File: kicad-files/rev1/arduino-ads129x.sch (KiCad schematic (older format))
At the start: 186 parts

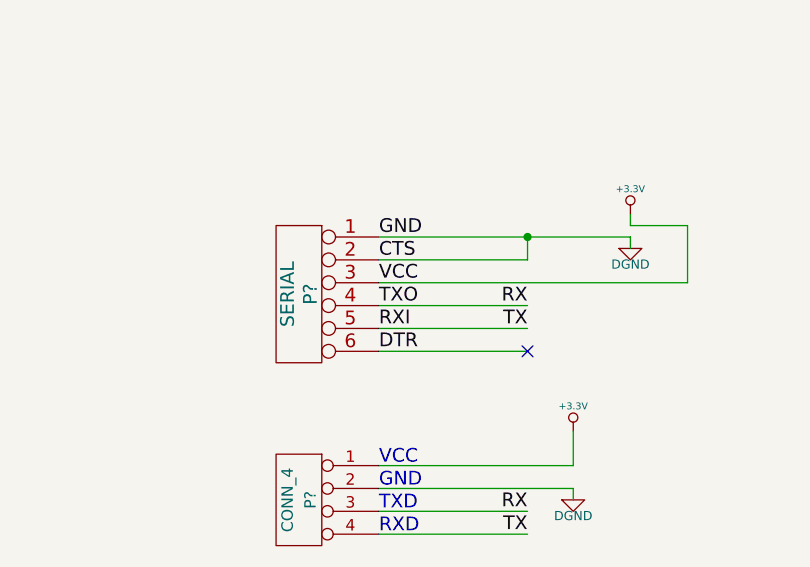
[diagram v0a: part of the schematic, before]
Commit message: replace serial port net-labels with plain text
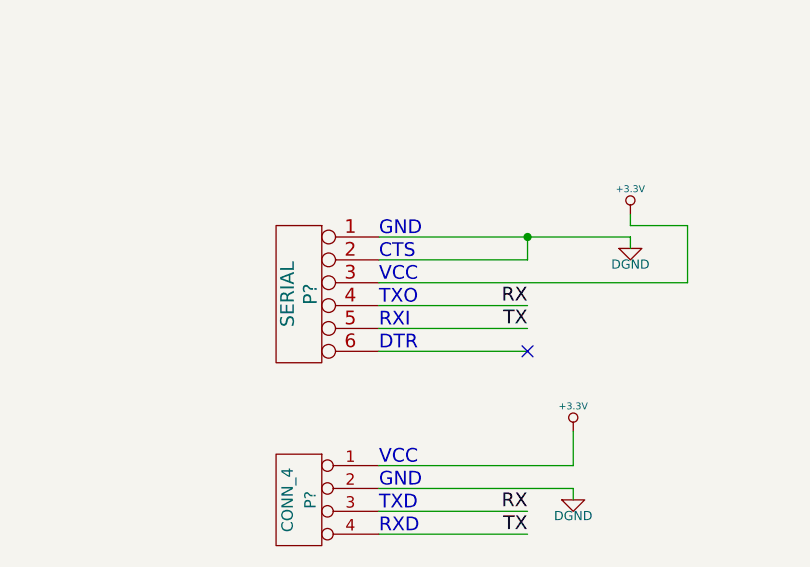
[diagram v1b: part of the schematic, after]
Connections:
- net labels removed: CTS, DTR, RXI, TXO, VCC
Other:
- note added: "CTS"
- note added: "DTR"
- note added: "RXI"
- note added: "TXO"
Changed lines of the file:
@@
-EESchema Schematic File Version 2  date Sat 18 May 2013 03:09:57 PM CEST
+EESchema Schematic File Version 2  date Sat 18 May 2013 03:14:03 PM CEST
 LIBS:power
 LIBS:device
@@
 Comment4 ""
 $EndDescr
+Text Notes 13000 11950 0    60   ~ 0
+DTR
+Text Notes 13000 11850 0    60   ~ 0
+RXI
+Text Notes 13000 11750 0    60   ~ 0
+TXO
+Text Notes 13000 11650 0    60   ~ 0
+VCC
+Text Notes 13000 11550 0    60   ~ 0
+CTS
+Text Notes 13000 11450 0    60   ~ 0
+GND
 Text Label 13650 12750 2    60   ~ 0
 TX
@@
 Text Notes 13000 12450 0    60   ~ 0
 VCC
-Text Label 13000 11450 0    60   ~ 0
-GND
 $Comp
 L CONN_4 P?
@@
 RX
 NoConn ~ 13650 11950
-Text Label 13000 11950 0    60   ~ 0
-DTR
-Text Label 13000 11850 0    60   ~ 0
-RXI
-Text Label 13000 11750 0    60   ~ 0
-TXO
-Text Label 13000 11650 0    60   ~ 0
-VCC
-Text Label 13000 11550 0    60   ~ 0
-CTS
 Text Label 17000 14450 0    60   ~ 0
 RX

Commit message: connect ADS129x to SAM3X
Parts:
- added R? (x4): 10k, symbol R
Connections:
- net labels added: ADS129x_CLK, ADS129x_CLKSEL, ADS129x_CS, ADS129x_DRDY, ADS129x_GPIO1, ADS129x_GPIO2, ADS129x_GPIO3, ADS129x_GPIO4, ADS129x_PWDN, ADS129x_RESET, ADS129x_START, MISO, MOSI, SPCK
- wire segments 678 -> 709
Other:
- note added: "TODO: How do we get the clock divided correctly?"

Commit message: connect ADS129x CLK to SAM3X PA2
 PA2 is labeled AD7 in the Arduino Due schematic
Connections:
- wire segments 709 -> 710
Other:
- note removed: "TODO: How do we get the clock divided correctly?"

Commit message: add yellow and green LEDs for each channel
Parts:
- added D? (x16): LED, symbol LED
- added R? (x8): 68, symbol R
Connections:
- net labels added: GREEN_1, GREEN_2, GREEN_3, GREEN_4, GREEN_5, GREEN_6, GREEN_7, GREEN_8, YELLOW_1, YELLOW_2, YELLOW_3, YELLOW_4, YELLOW_5, YELLOW_6, YELLOW_7, YELLOW_8
- wire segments 710 -> 775

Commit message: add MAYBE note regarding connectors and ground lines
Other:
- note added: "MAYBE double the\nconnectors to \nallow ground lines\ninbetween\nthe signal lines"
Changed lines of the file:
@@
-EESchema Schematic File Version 2  date Sun 19 May 2013 10:32:49 AM CEST
+EESchema Schematic File Version 2  date Sat 25 May 2013 01:05:47 PM CEST
 LIBS:power
 LIBS:device
@@
 Sheet 1 1
 Title ""
-Date "19 may 2013"
+Date "25 may 2013"
 Rev ""
 Comp ""
@@
 Comment4 ""
 $EndDescr
+Text Notes 700  4400 0    60   ~ 0
+MAYBE double the\nconnectors to \nallow ground lines\ninbetween\nthe signal lines
 Text Label 22400 16750 1    60   ~ 0
 GREEN_8

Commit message: make arduino-ads129x header match patch-shield header
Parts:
- removed P?: CONN_10X2, symbol CONN_10X2
- added P?: CONN_20X2, symbol CONN_20X2
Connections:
- net labels removed: VIRTUALGND
- wire segments 775 -> 801
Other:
- note removed: "MAYBE double the\nconnectors to \nallow ground lines\ninbetween\nthe signal lines"

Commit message: move LEDs to patch-shield
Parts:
- removed D? (x16): LED, symbol LED
- removed R? (x8): 68, symbol R
- R?: value 1k -> 560
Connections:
- net labels removed: GREEN_1, GREEN_2, GREEN_3, GREEN_4, GREEN_5, GREEN_6, GREEN_7, GREEN_8, YELLOW_1, YELLOW_2, YELLOW_3, YELLOW_4, YELLOW_5, YELLOW_6, YELLOW_7, YELLOW_8
- wire segments 801 -> 965

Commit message: added shift-out register for LEDs
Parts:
- added P?: CONN_4X2, symbol CONN_4X2
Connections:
- net labels added: LED_LATCH_CLK, LED_OUTPUT_ENABLE_INPUT, LED_SERIAL, LED_SHIFT_REG_CLEAR, LED_SHIFT_REG_CLK
- wire segments 965 -> 984
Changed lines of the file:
@@
-EESchema Schematic File Version 2  date Sat 25 May 2013 04:37:08 PM CEST
+EESchema Schematic File Version 2  date Sat 25 May 2013 05:49:57 PM CEST
 LIBS:power
 LIBS:device
@@
 Comment4 ""
 $EndDescr
+Text Label 16050 12350 0    60   ~ 0
+LED_SERIAL
+Text Label 16050 12500 0    60   ~ 0
+LED_SHIFT_REG_CLK
+Text Label 16050 12650 0    60   ~ 0
+LED_SHIFT_REG_CLEAR
+Text Label 16050 12800 0    60   ~ 0
+LED_LATCH_CLK
+Text Label 16050 13250 0    60   ~ 0
+LED_OUTPUT_ENABLE_INPUT
+Wire Wire Line
+	16050 12800 17700 12800
+Wire Wire Line
+	17700 12500 16050 12500
+Wire Wire Line
+	17700 12350 16050 12350
+Wire Wire Line
+	17700 12650 16050 12650
+Wire Wire Line
+	16050 13250 17700 13250
+$Comp
+L CONN_4X2 P?
+U 1 1 51A0DAEE
+P 5650 11750
+F 0 "P?" H 5650 12000 50  0000 C CNN
+F 1 "CONN_4X2" V 5650 11750 40  0000 C CNN
+	1    5650 11750
+	1    0    0    -1
+$EndComp
+$Comp
+L +3.3V #PWR?
+U 1 1 51A0DAED
+P 5150 11250
+F 0 "#PWR?" H 5150 11210 30  0001 C CNN
+F 1 "+3.3V" H 5150 11360 30  0000 C CNN
+	1    5150 11250
+	1    0    0    -1
+$EndComp
+Text Label 6466 11800 0    60   ~ 0
+LED_OUTPUT_ENABLE_INPUT
+Text Label 7008 11700 0    60   ~ 0
+LED_LATCH_CLK
+Text Label 3600 11900 0    60   ~ 0
+LED_SHIFT_REG_CLEAR
+Text Label 3600 11800 0    60   ~ 0
+LED_SHIFT_REG_CLK
+Text Label 3600 11700 0    60   ~ 0
+LED_SERIAL
+$Comp
+L DGND #PWR?
+U 1 1 51A0DAEC
+P 6150 12350
+F 0 "#PWR?" H 6150 12350 40  0001 C CNN
+F 1 "DGND" H 6150 12280 40  0000 C CNN
+	1    6150 12350
+	1    0    0    -1
+$EndComp
+$Comp
+L PWR_FLAG #FLG?
+U 1 1 51A0DAEB
+P 4900 11400
+F 0 "#FLG?" H 4900 11495 30  0001 C CNN
+F 1 "PWR_FLAG" H 4900 11580 30  0000 C CNN
+	1    4900 11400
+	1    0    0    -1
+$EndComp
+$Comp
+L PWR_FLAG #FLG?
+U 1 1 51A0DAEA
+P 5900 12250
+F 0 "#FLG?" H 5900 12345 30  0001 C CNN
+F 1 "PWR_FLAG" H 5900 12430 30  0000 C CNN
+	1    5900 12250
+	1    0    0    -1
+$EndComp
+Connection ~ 5150 11500
+Wire Wire Line
+	4900 11500 5150 11500
+Wire Wire Line
+	4900 11400 4900 11500
+Wire Wire Line
+	6150 11600 6150 12350
+Wire Wire Line
+	7700 11800 6050 11800
+Wire Wire Line
+	5250 11900 3600 11900
+Wire Wire Line
+	5250 11700 3600 11700
+Wire Wire Line
+	5250 11800 3600 11800
+Wire Wire Line
+	7700 11700 6050 11700
+Wire Wire Line
+	5150 11600 5150 11250
+Wire Wire Line
+	5250 11600 5150 11600
+Wire Wire Line
+	6050 11600 6150 11600
+Wire Wire Line
+	6050 11900 6150 11900
+Connection ~ 6150 11900
+Wire Wire Line
+	5900 12300 5900 12250
+Wire Wire Line
+	6150 12300 5900 12300
+Connection ~ 6150 12300
 Connection ~ 2150 4900
 Wire Wire Line
